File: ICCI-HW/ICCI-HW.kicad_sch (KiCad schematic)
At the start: 0 parts

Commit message: start layout
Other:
- note removed: "- solve small errors on DRC"
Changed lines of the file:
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@@
     (stroke (width 0) (type default) (color 0 0 0 0))
-  )
-  (text "- solve small errors on DRC" (at 112.395 144.145 0)
-    (effects (font (size 3 3)) (justify left bottom))
   )
   (sheet (at 131.445 69.85) (size 38.1 51.435) (fields_autoplaced)
@@
       (reference "#PWR0117") (unit 1) (value "+BATT") (footprint "")
     )
+    (path "/5edebedc-f41c-4f1f-9f90-5bb7df590118/a15c4e38-11f1-4bac-822b-4b4e52834357"
+      (reference "#PWR0118") (unit 1) (value "+3V3") (footprint "")
+    )
+    (path "/5edebedc-f41c-4f1f-9f90-5bb7df590118/eda7096f-7ab4-4a98-a62f-1666eae1d3b2"
+      (reference "#PWR0119") (unit 1) (value "GND") (footprint "")
+    )
     (path "/c01df0d0-40d4-4f5b-bf2f-5193fe038d8f/d705c027-5032-41c6-9969-7321e692dae2"
       (reference "#PWR0201") (unit 1) (value "GND") (footprint "")
@@
       (reference "#PWR0223") (unit 1) (value "GND") (footprint "")
     )
+    (path "/c01df0d0-40d4-4f5b-bf2f-5193fe038d8f/dd598f77-4e51-4157-9d94-9d6481f76c50"
+      (reference "#PWR0224") (unit 1) (value "GND") (footprint "")
+    )
     (path "/8c92c57f-d331-41ba-8fa9-9179d95410d1/063eaec5-00f3-429a-8ceb-98e35c2b51a1"
       (reference "#PWR0301") (unit 1) (value "+1V8") (footprint "")
@@
       (reference "#PWR0416") (unit 1) (value "+3V3") (footprint "")
     )
-    (path "/1c257f8f-2137-47e2-9ced-0ed4433361c2/629d18d3-9933-4e34-8dde-ff63afd8e67b"
-      (reference "#PWR0417") (unit 1) (value "+3V3") (footprint "")
-    )
-    (path "/1c257f8f-2137-47e2-9ced-0ed4433361c2/7b60b961-7556-43c2-a734-9a4284f2a036"
-      (reference "#PWR0418") (unit 1) (value "GND") (footprint "")
-    )
     (path "/1c257f8f-2137-47e2-9ced-0ed4433361c2/a90800df-b28f-4ea8-beb1-dc5c8828a828"
       (reference "#PWR0420") (unit 1) (value "GND") (footprint "")
@@
       (reference "J201") (unit 1) (value "USB_C_Receptacle_USB2.0") (footprint "ICCI-LIB:USB_C_Receptacle_Amphenol_12401548E4-2A")
     )
-    (path "/1c257f8f-2137-47e2-9ced-0ed4433361c2/829a4c91-9d91-42c1-94db-8bc078f54a3a"
-      (reference "J401") (unit 1) (value "EXP0") (footprint "Connector_PinHeader_2.54mm:PinHeader_1x04_P2.54mm_Vertical")
-    )
-    (path "/1c257f8f-2137-47e2-9ced-0ed4433361c2/0f62f2af-1ce0-4112-8c6c-4a975da48092"
-      (reference "J402") (unit 1) (value "EXP1") (footprint "Connector_PinHeader_2.54mm:PinHeader_1x04_P2.54mm_Vertical")
+    (path "/1c257f8f-2137-47e2-9ced-0ed4433361c2/325d0195-9772-4cde-a789-f94dd0a78295"
+      (reference "J401") (unit 1) (value "EXP") (footprint "Connector_PinSocket_2.54mm:PinSocket_2x03_P2.54mm_Horizontal")
     )
     (path "/1c257f8f-2137-47e2-9ced-0ed4433361c2/4714646e-78fd-49d7-89a9-7c30a658200e"
       (reference "J403") (unit 1) (value "DM3AT-SF-PEJM5") (footprint "ICCI-LIB:ICCI_microSD_HC_Hirose_DM3AT-SF-PEJM5")
     )
-    (path "/5edebedc-f41c-4f1f-9f90-5bb7df590118/4318ab19-1190-4b09-8f82-cbcf46c82f42"
-      (reference "J501") (unit 1) (value "JTAG") (footprint "Connector_PinHeader_2.54mm:PinHeader_1x04_P2.54mm_Vertical")
+    (path "/5edebedc-f41c-4f1f-9f90-5bb7df590118/0895574d-8553-4389-bb8c-d482793ef26c"
+      (reference "J501") (unit 1) (value "JTAG") (footprint "ICCI-LIB:JST_B6B-XH-A")
+    )
+    (path "/5edebedc-f41c-4f1f-9f90-5bb7df590118/115be9a1-441b-4b5d-8ce2-2c9a78a30fbc"
+      (reference "JP501") (unit 1) (value "SolderJumper_3_Bridged12") (footprint "Jumper:SolderJumper-3_P1.3mm_Open_RoundedPad1.0x1.5mm_NumberLabels")
+    )
+    (path "/5edebedc-f41c-4f1f-9f90-5bb7df590118/b14add3c-33d5-4ef2-8b23-6a5b974a5c9f"
+      (reference "JP502") (unit 1) (value "SolderJumper_3_Bridged12") (footprint "Jumper:SolderJumper-3_P1.3mm_Open_RoundedPad1.0x1.5mm_NumberLabels")
+    )
+    (path "/5edebedc-f41c-4f1f-9f90-5bb7df590118/b94e2087-fcc6-4652-8986-051fc5143dcc"
+      (reference "JP503") (unit 1) (value "SolderJumper_3_Bridged12") (footprint "Jumper:SolderJumper-3_P1.3mm_Open_RoundedPad1.0x1.5mm_NumberLabels")
     )
     (path "/cae5ab82-da76-4670-8a36-68f75cc70c4e/c8fecb44-a43c-4b45-a2af-14b55155f619"
@@
       (reference "L602") (unit 1) (value "1.5u") (footprint "ICCI-LIB:ICCI_L_Coilcraft_XxL4040")
     )
-    (path "/c01df0d0-40d4-4f5b-bf2f-5193fe038d8f/75264ed2-ae1b-4a87-a4ff-85d28504968e"
-      (reference "NT201") (unit 1) (value "NetTie_2") (footprint "NetTie:NetTie-2_SMD_Pad0.5mm")
-    )
     (path "/c01df0d0-40d4-4f5b-bf2f-5193fe038d8f/ed006e6b-4399-4896-a99b-2ecddea09a37"
       (reference "Q201") (unit 1) (value "PDTC114Y") (footprint "Package_TO_SOT_SMD:SOT-23")
@@
       (reference "Q203") (unit 1) (value "NX7002AK") (footprint "Package_TO_SOT_SMD:SOT-23")
     )
+    (path "/c01df0d0-40d4-4f5b-bf2f-5193fe038d8f/408b91c6-990d-4a3e-b0e1-176b6668c2f6"
+      (reference "Q204") (unit 1) (value "NX7002AK") (footprint "Package_TO_SOT_SMD:SOT-23")
+    )
     (path "/1c257f8f-2137-47e2-9ced-0ed4433361c2/45508684-19ee-4ae3-9baa-ede8466189d8"
       (reference "Q401") (unit 1) (value "RZM001P02") (footprint "ICCI-LIB:RZM001P02")
@@
     )
     (path "/5edebedc-f41c-4f1f-9f90-5bb7df590118/c55efee1-81ff-4534-a65b-d90a60e9334a"
-      (reference "TP501") (unit 1) (value "TP_3V3") (footprint "TestPoint:TestPoint_Plated_Hole_D2.0mm")
+      (reference "TP501") (unit 1) (value "TP_3V3") (footprint "TestPoint:TestPoint_THTPad_D1.5mm_Drill0.7mm")
     )
     (path "/5edebedc-f41c-4f1f-9f90-5bb7df590118/ed80421b-5207-4022-9417-7162a4ab2395"
-      (reference "TP502") (unit 1) (value "TP_Li_Ion") (footprint "TestPoint:TestPoint_Plated_Hole_D2.0mm")
+      (reference "TP502") (unit 1) (value "TP_Li_Ion") (footprint "TestPoint:TestPoint_THTPad_D1.5mm_Drill0.7mm")
     )
     (path "/5edebedc-f41c-4f1f-9f90-5bb7df590118/5c4394ed-ec7b-430a-bc6b-e4e18d3e04f4"
-      (reference "TP503") (unit 1) (value "TP_VSYS") (footprint "TestPoint:TestPoint_Plated_Hole_D2.0mm")
+      (reference "TP503") (unit 1) (value "TP_VSYS") (footprint "TestPoint:TestPoint_THTPad_D1.5mm_Drill0.7mm")
     )
     (path "/5edebedc-f41c-4f1f-9f90-5bb7df590118/d604f14b-59c7-46e2-9d9e-7587a661be6d"
-      (reference "TP504") (unit 1) (value "TP_GND") (footprint "TestPoint:TestPoint_Plated_Hole_D2.0mm")
+      (reference "TP504") (unit 1) (value "TP_GND") (footprint "TestPoint:TestPoint_THTPad_D1.5mm_Drill0.7mm")
     )
     (path "/5edebedc-f41c-4f1f-9f90-5bb7df590118/bee44298-9d1e-4f8e-892f-66dc26c3ccbd"
-      (reference "TP505") (unit 1) (value "TP_3V_BAT") (footprint "TestPoint:TestPoint_Plated_Hole_D2.0mm")
-    )
-    (path "/5edebedc-f41c-4f1f-9f90-5bb7df590118/89d0dd12-5360-4b8c-ba52-c8aac480538d"
-      (reference "TP506") (unit 1) (value "TP_CLK/TP") (footprint "TestPoint:TestPoint_Plated_Hole_D2.0mm")
+      (reference "TP505") (unit 1) (value "TP_3V_BAT") (footprint "TestPoint:TestPoint_THTPad_D1.5mm_Drill0.7mm")
     )
     (path "/5edebedc-f41c-4f1f-9f90-5bb7df590118/99400e69-7804-4e3e-8183-e1f5cd3c0bef"
-      (reference "TP507") (unit 1) (value "TP_VBUS") (footprint "TestPoint:TestPoint_Plated_Hole_D2.0mm")
+      (reference "TP507") (unit 1) (value "TP_VBUS") (footprint "TestPoint:TestPoint_THTPad_D1.5mm_Drill0.7mm")
     )
     (path "/5edebedc-f41c-4f1f-9f90-5bb7df590118/ee873cdc-baa5-49a8-8c53-5ae5381259fa"
-      (reference "TP508") (unit 1) (value "TP_1V8") (footprint "TestPoint:TestPoint_Plated_Hole_D2.0mm")
+      (reference "TP508") (unit 1) (value "TP_1V8") (footprint "TestPoint:TestPoint_THTPad_D1.5mm_Drill0.7mm")
     )
     (path "/c01df0d0-40d4-4f5b-bf2f-5193fe038d8f/6c354d53-cabe-4a6a-9340-609d745500f5"
@@
     )
     (path "/8c92c57f-d331-41ba-8fa9-9179d95410d1/1d3dcc0d-9cd5-48cb-9abf-0ee2d01f2f8d"
-      (reference "U301") (unit 1) (value "DS18B20") (footprint "Package_TO_SOT_THT:TO-92_Inline")
+      (reference "U301") (unit 1) (value "DS18B20") (footprint "ICCI-LIB:DS18B20 Hor.")
     )
     (path "/8c92c57f-d331-41ba-8fa9-9179d95410d1/89540e6d-712a-40b7-88ac-0d590ae509d6"

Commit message: layout PCB V1.0
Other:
- sheet AUX + Peripherals ports: added ~{GPS_RST}; removed ~{GPS_RESET}
- sheet ESP ports: added ~{GPS_RST}; removed ~{GPS_RESET}
- title: ICCI (Iperspectral Camera Calibration Instrument) -> LAITS (Light Analysis Iot porTable Spectrometer)
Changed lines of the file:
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@@
   (paper "A4")
   (title_block
-    (title "ICCI (Iperspectral Camera Calibration Instrument)")
+    (title "LAITS (Light Analysis Iot porTable Spectrometer)")
     (date "2022-07-14")
-    (rev "BETA")
+    (rev "1.0")
     (company "Simone Tollardo")
   )
@@
       (effects (font (size 1.27 1.27)) (justify right))
     )
-    (pin "~{GPS_RESET}" input (at 169.545 107.315 0)
+    (pin "~{GPS_RST}" input (at 169.545 107.315 0)
       (effects (font (size 1.27 1.27)) (justify right))
     )
@@
       (effects (font (size 1.27 1.27)) (justify left))
     )
-    (pin "~{GPS_RESET}" output (at 173.99 107.315 180)
-      (effects (font (size 1.27 1.27)) (justify left))
-    )
+    (pin "~{GPS_RST}" output (at 173.99 107.315 180)
+      (effects (font (size 1.27 1.27)) (justify left))
+    )

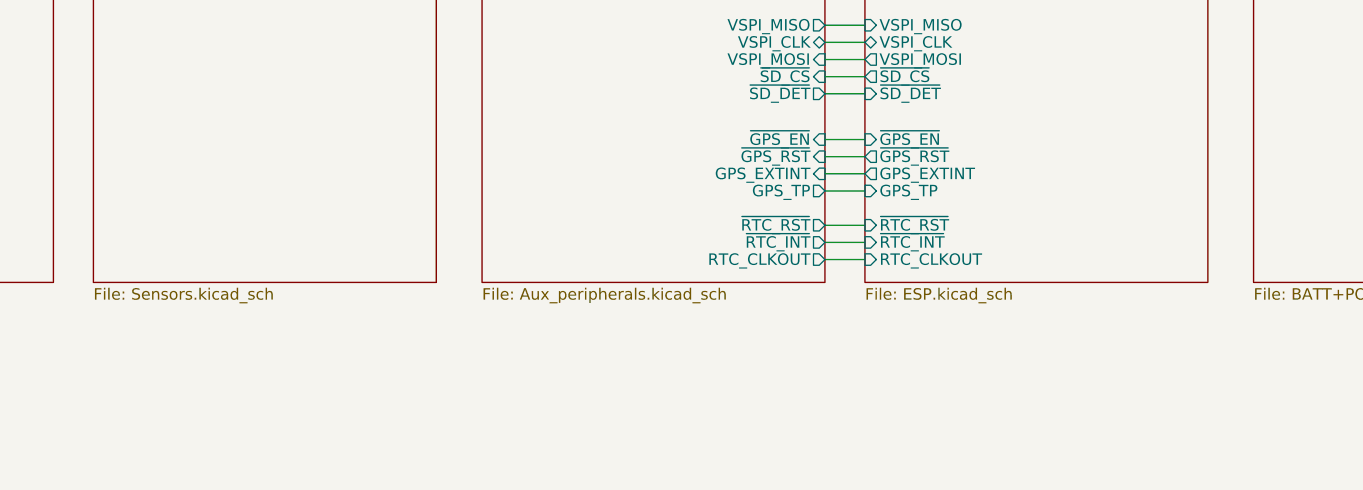
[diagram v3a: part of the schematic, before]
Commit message: hw: fix missing contact from SYS to SYSA on MAX77960
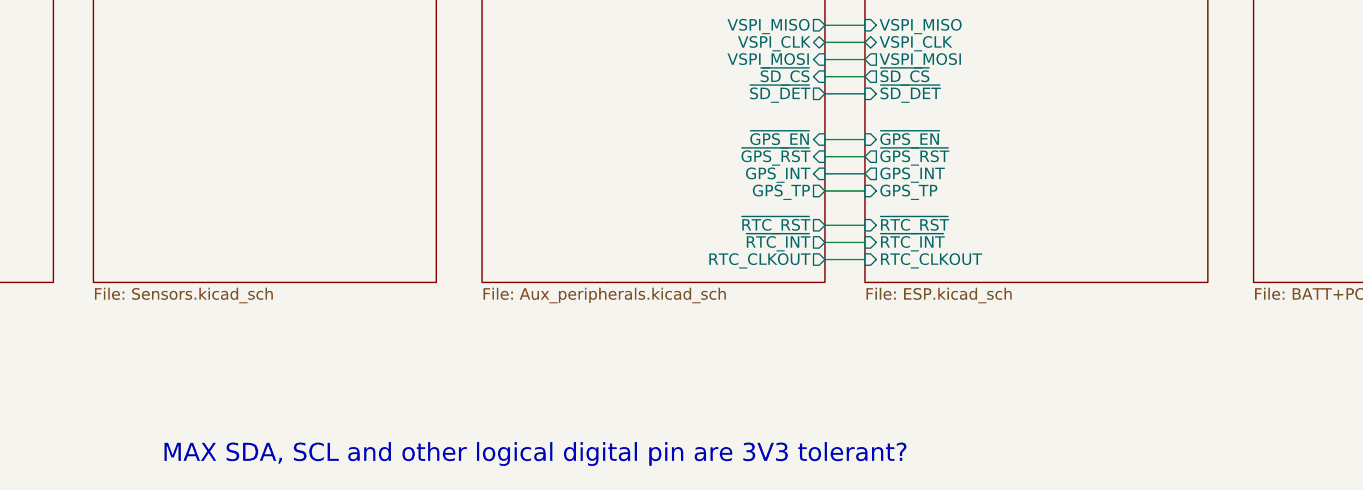
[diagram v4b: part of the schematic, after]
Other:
- sheet AUX + Peripherals ports: added GPS_INT; removed GPS_EXTINT
- sheet ESP ports: added GPS_INT; removed GPS_EXTINT
- note added: "MAX SDA, SCL and other logical digital pin are 3V3 tolerant?"
